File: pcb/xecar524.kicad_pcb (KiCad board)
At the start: 2 copper layers, 63.8 x 88.9 mm, 40 parts, among them J1 JTAG, J2 PROG, J3 Conn_02x02_Odd_Even, U1 MCP1703A-3302_SOT89, U2 Atari_XE_Cartridge_Connector, U3 XC95144XL-TQ100, U4 SST39VF040

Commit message: PCB: Exchange cfg signals
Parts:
- removed REF**: OSHW-Symbol_6.7x6mm_Copper, Symbol:OSHW-Symbol_6.7x6mm_Copper
- D1: value LED -> KP-2012SGC
- D2: value LED -> FYLS-0805URC
- D3: value LED -> KP-2012SYC
- R1: value 1k -> 100
- R14: value 1k -> 470
- R15: value 1k -> 220
- moved R16 2.54 mm to (140.1, 121.9)
- moved R17 2.54 mm to (140.1, 124.5)
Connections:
- J3 pad 1: CFG0 -> CFG1
- J3 pad 3: CFG1 -> CFG0
- U3 pad 37: CFG1 -> CFG0
- U3 pad 39: CFG0 -> CFG1
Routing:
- net CFG1: track 63.8 -> 63.2 mm
- net CFG0: track 63.2 -> 63.8 mm

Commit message: PCB: Resize
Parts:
- moved R14 1.54 mm to (126.0, 74.9)
- moved R15 1.54 mm to (126.0, 77.0)
- moved D1 0.78 mm to (121.2, 68.0)
- moved R1 0.75 mm to (121.2, 65.5)
- moved D2 0.70 mm to (121.2, 74.9)
- moved D3 0.70 mm to (121.2, 77.0)
- moved R2 0.53 mm to (133.8, 117.2)
- moved R3 0.53 mm to (133.8, 112.1)
- moved R4 0.53 mm to (133.8, 109.6)
- moved R5 0.53 mm to (133.8, 107.0)
- moved R6 0.53 mm to (133.8, 104.5)
- moved J2 0.50 mm to (127.0, 100.0)
- moved J1 0.50 mm to (127.0, 117.2)
- moved J3 0.46 mm to (132.5, 124.5)
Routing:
- net GND: track 50.8 -> 43.0 mm
- net +3V3: track 221.8 -> 219.0 mm
- net Net-(R15-Pad1): track 17.9 -> 16.4 mm
- net Net-(R14-Pad1): track 17.8 -> 16.2 mm
- net Net-(D3-Pad1): track 1.89 -> 2.72 mm
- net Net-(D2-Pad1): track 1.89 -> 2.72 mm
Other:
- board size 63.8 x 88.9 mm -> 62.8 x 89.4 mm

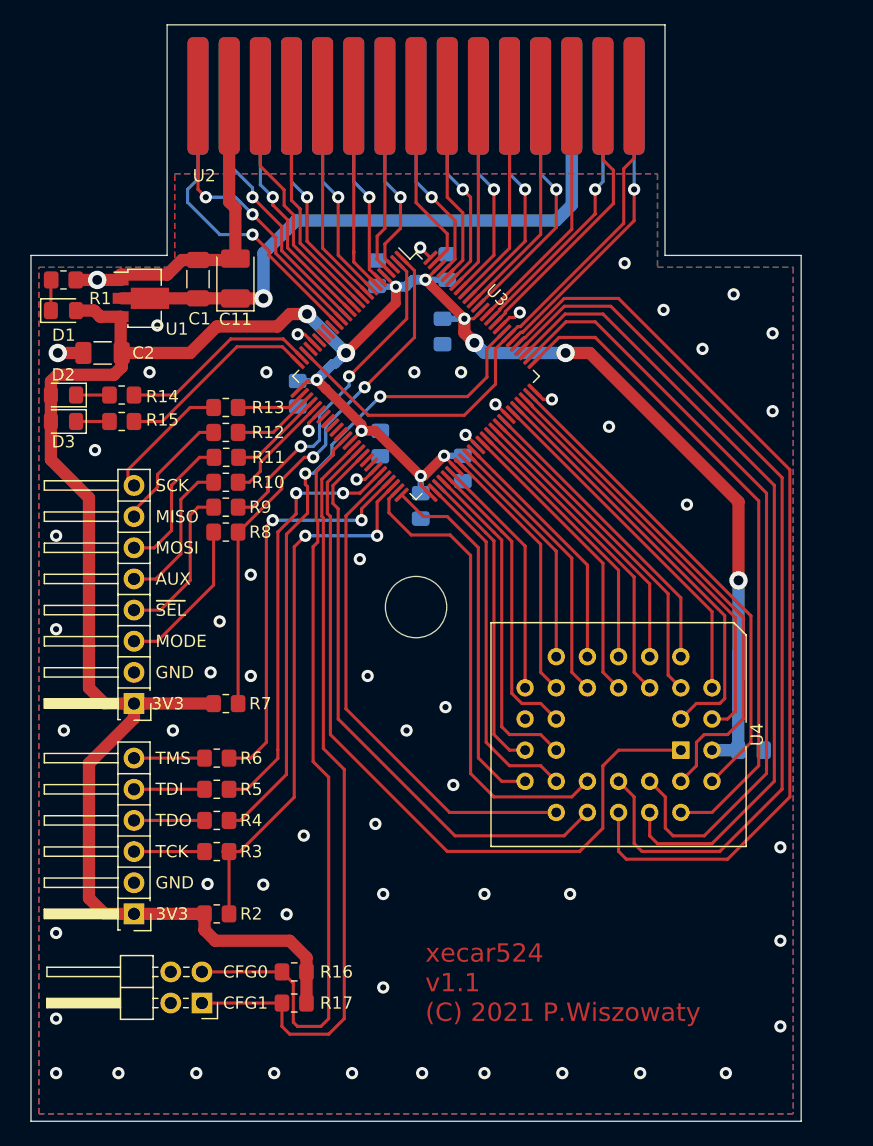
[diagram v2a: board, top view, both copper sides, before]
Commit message: PCB, PLD: Integrate R-Time 8 emulator
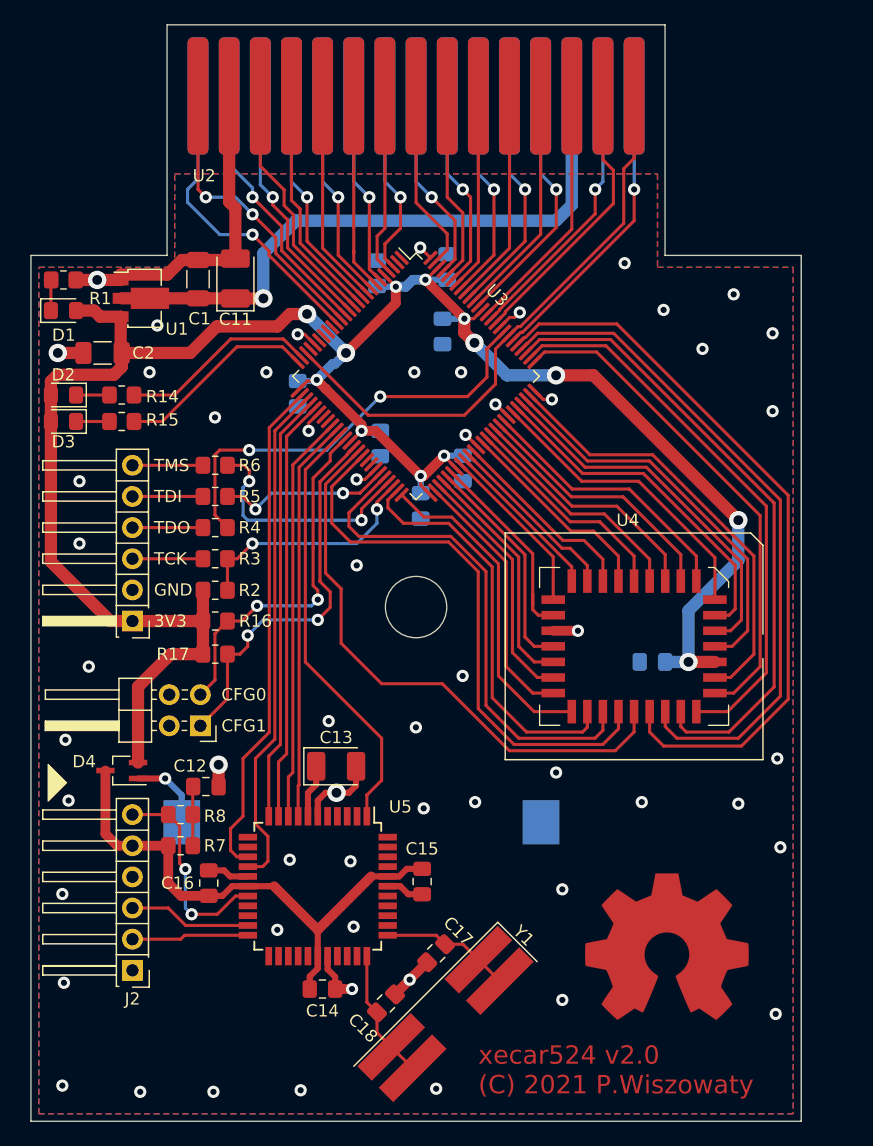
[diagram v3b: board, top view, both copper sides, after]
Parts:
- removed R10, R11, R12, R13, R9: 100, Resistor_SMD:R_0805_2012Metric_Pad1.20x1.40mm_HandSolder
- added BT1: CR2032, Miscellaneous:BatteryHolder_Connfly_DS1092-10, B.Cu at (145.5, 109.7)
- added C12: 100nF, Capacitor_SMD:C_0805_2012Metric_Pad1.18x1.45mm_HandSolder, F.Cu at (132.9, 106.8)
- added C13: 10uF, Capacitor_Tantalum_SMD:CP_EIA-3528-12_Kemet-T_Pad1.50x2.35mm_HandSolder, F.Cu at (143.5, 105.2)
- added C14: 100nF, Capacitor_SMD:C_0805_2012Metric_Pad1.18x1.45mm_HandSolder, F.Cu at (142.4, 123.3)
- added C15: 100nF, Capacitor_SMD:C_0805_2012Metric_Pad1.18x1.45mm_HandSolder, F.Cu at (150.5, 114.6)
- added C16: 100nF, Capacitor_SMD:C_0805_2012Metric_Pad1.18x1.45mm_HandSolder, F.Cu at (133.1, 114.7)
- added C17: 10pF, Capacitor_SMD:C_0805_2012Metric_Pad1.18x1.45mm_HandSolder, F.Cu at (151.6, 120.4)
- added C18: 10pF, Capacitor_SMD:C_0805_2012Metric_Pad1.18x1.45mm_HandSolder, F.Cu at (147.5, 124.5)
- added D4: 1PS70SB15, Package_TO_SOT_SMD:SOT-323_SC-70_Handsoldering, F.Cu at (126.0, 105.5)
- added REF**: OSHW-Symbol_13.4x12mm_Copper, Symbol:OSHW-Symbol_13.4x12mm_Copper, F.Cu at (170.4, 119.9)
- added U5: PIC24FJ32GA004-I/PT, Package_QFP:TQFP-44_10x10mm_P0.8mm, F.Cu at (142.0, 114.9)
- added Y1: 32768, Crystal:Crystal_SMD_SeikoEpson_MC406-4Pin_9.6x4.1mm_HandSoldering, F.Cu at (152.4, 125.3)
- J2: value PROG -> ICSP; footprint Connector_PinHeader_2.54mm:PinHeader_1x08_P2.54mm_Horizontal_HighProfile -> Connector_PinHeader_2.54mm:PinHeader_1x06_P2.54mm_Horizontal_HighProfile
- R15: value 220 -> 470
- R8: value 100 -> 470
- U4: footprint Package_LCC:PLCC-32_THT-Socket -> Miscellaneous:PLCC-32_SMD-Socket
- moved R16 29.3 mm to (133.6, 93.3), turned to 0 degrees
- moved R17 29.2 mm to (133.6, 96.0), turned to 0 degrees
- moved R2 26.4 mm to (133.6, 90.8)
- moved J1 23.9 mm to (126.9, 93.3)
- moved R3 23.9 mm to (133.6, 88.2)
- moved R5 23.9 mm to (133.6, 83.2)
- moved R4 23.9 mm to (133.6, 85.7)
- moved R6 23.9 mm to (133.6, 80.6)
- moved R8 23.3 mm to (130.8, 109.1), turned to 0 degrees
- moved J3 22.6 mm to (132.4, 101.9)
- moved J2 21.8 mm to (126.9, 121.8)
- moved R7 12.2 mm to (130.8, 111.6), turned to 0 degrees
- moved C9 10.8 mm to (169.3, 96.6), turned to 180 degrees
- moved U4 9.28 mm to (167.8, 95.4)
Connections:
- J2 pad 1: +3V3 -> Net-(J2-Pad1)
- J2 pad 2: GND -> PGC
- J2 pad 3: Net-(J2-Pad3) -> PGD
- J2 pad 4: Net-(J2-Pad4) -> GND
- J2 pad 5: Net-(J2-Pad5) -> VDD
- J2 pad 6: Net-(J2-Pad6) -> MCLR
- R7 pad 1: MODE -> VDD
- R7 pad 2: +3V3 -> Net-(C12-Pad1)
- R8 pad 1: MODE -> MCLR
- R8 pad 2: Net-(J2-Pad3) -> Net-(C12-Pad1)
- U3 pad 1: MODE -> Net-(U3-Pad1)
- U3 pad 2: SEL# -> Net-(U3-Pad2)
- U3 pad 27: SCK -> PMWR
- U3 pad 28: MISO -> PMCS1
- U3 pad 29: MOSI -> PMRD
- U3 pad 30: AUX -> PMD0
- U3 pad 34: Net-(U3-Pad34) -> PMD1
- U3 pad 35: Net-(U3-Pad35) -> PMD2
- U3 pad 36: Net-(U3-Pad36) -> PMD3
- U3 pad 40: ROM_A18 -> ROM_A11
- U3 pad 41: ROM_A10 -> OE#
- U3 pad 46: ROM_D7 -> ROM_A10
- U3 pad 49: OE# -> CE#
- U3 pad 50: ROM_D6 -> ROM_D7
- U3 pad 52: CE# -> ROM_D6
- U3 pad 53: ROM_D4 -> ROM_D5
- U3 pad 54: ROM_D5 -> ROM_D4
- U3 pad 56: ROM_D1 -> ROM_D2
- U3 pad 58: ROM_D2 -> ROM_D1
- U3 pad 73: WE# -> ROM_A18
- U3 pad 74: ROM_A17 -> WE#
- U3 pad 76: ROM_A14 -> ROM_A17
- U3 pad 77: ROM_A13 -> ROM_A14
- U3 pad 78: ROM_A8 -> ROM_A13
- U3 pad 79: ROM_A9 -> ROM_A8
- U3 pad 80: ROM_A11 -> ROM_A9
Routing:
- net VDD: track 0.00 -> 43.8 mm
- net MODE: track 43.2 -> 0.00 mm, vias 2 -> 0
- net PMCS1: track 0.00 -> 41.6 mm
- net PMWR: track 0.00 -> 41.2 mm
- net PMD3: track 0.00 -> 35.4 mm
- net +3V3: track 219.0 -> 183.8 mm, vias 12 -> 13
- net PMRD: track 0.00 -> 35.1 mm
- net PMD0: track 0.00 -> 34.5 mm
- net CFG0: track 63.3 -> 29.4 mm, vias 0 -> 2
- net PMD1: track 0.00 -> 33.4 mm
- net PMD2: track 0.00 -> 32.8 mm
- net CFG1: track 62.7 -> 31.8 mm, vias 0 -> 2
- net ROM_A18: track 63.1 -> 32.5 mm
- net ROM_A11: track 75.8 -> 47.1 mm
- net SEL#: track 27.7 -> 0.00 mm, vias 2 -> 0
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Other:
- board text added: "xecar524 v2.0 (C) 2021 P.Wiszowaty"
- board text removed: "AUX"
- board text removed: "MISO"
- board text removed: "MODE"
- board text removed: "MOSI"
- board text removed: "SCK"
- board text removed: "xecar524 v1.1 (C) 2021 P.Wiszowaty"
- board text removed: "~SEL~"

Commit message: PCB: Add connector for measuring deep sleep current
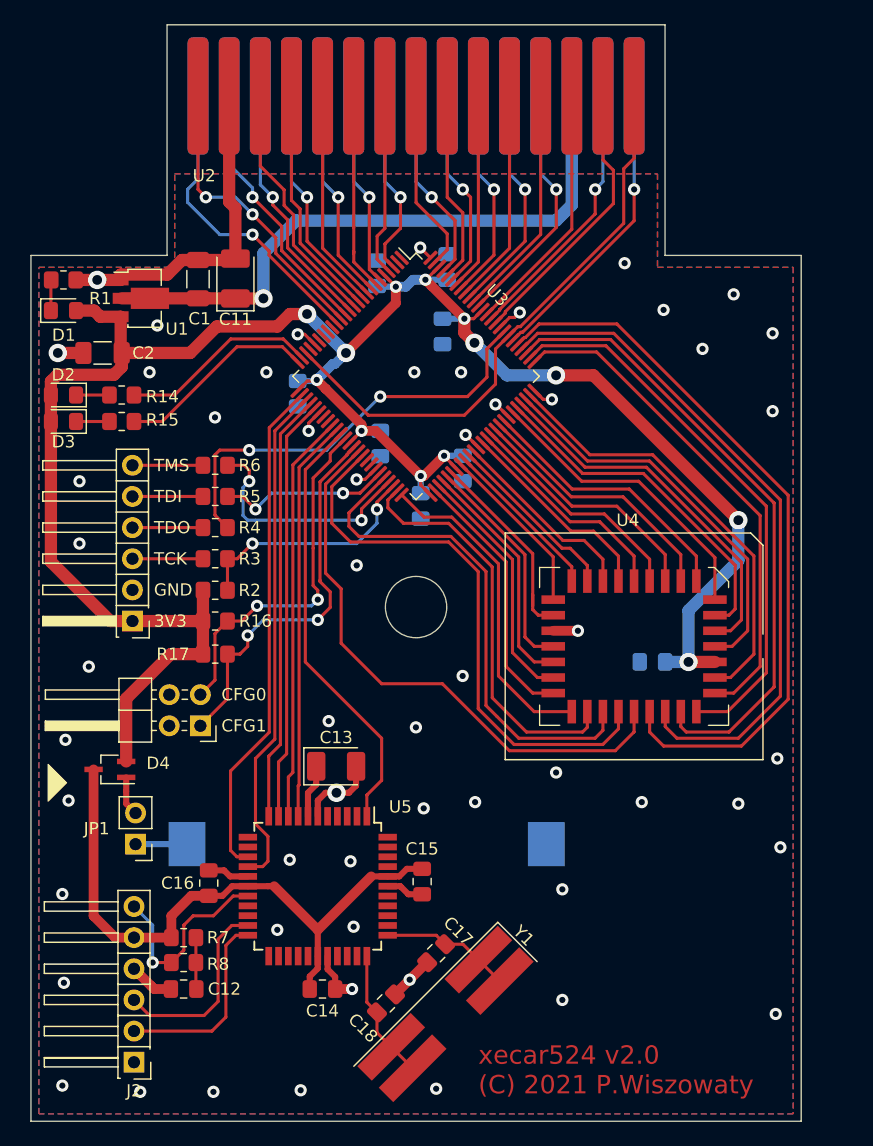
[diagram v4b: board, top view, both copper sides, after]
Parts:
- removed REF**: OSHW-Symbol_13.4x12mm_Copper, Symbol:OSHW-Symbol_13.4x12mm_Copper
- added JP1: Jumper_2_Bridged, Connector_PinHeader_2.54mm:PinHeader_1x02_P2.54mm_Vertical, F.Cu at (127.1, 111.5)
- C17, C18: value 10pF -> 15pF
- moved C12 16.6 mm to (131.0, 123.3), turned to 180 degrees
- moved R8 12.1 mm to (131.0, 121.2)
- moved R7 7.50 mm to (131.0, 119.1)
- moved J2 7.49 mm to (127.0, 129.3)
- moved BT1 1.83 mm to (146.0, 111.5)
- moved D4 0.97 mm to (125.0, 105.4)
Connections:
- D4 pad 1: Net-(BT1-Pad1) -> Net-(D4-Pad1)
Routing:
- net VDD: track 43.8 -> 50.9 mm
- net PGC: track 9.54 -> 15.9 mm
- net PGD: track 10.0 -> 15.8 mm
- net Net-(D4-Pad1): track 0.00 -> 3.22 mm
- net Net-(BT1-Pad1): track 6.35 -> 4.19 mm, vias 1 -> 0
- net GND: track 67.8 -> 69.7 mm, vias 57 -> 56
- net MCLR: track 17.0 -> 16.4 mm, vias 2 -> 1
- net Net-(C12-Pad1): track 4.84 -> 4.21 mm

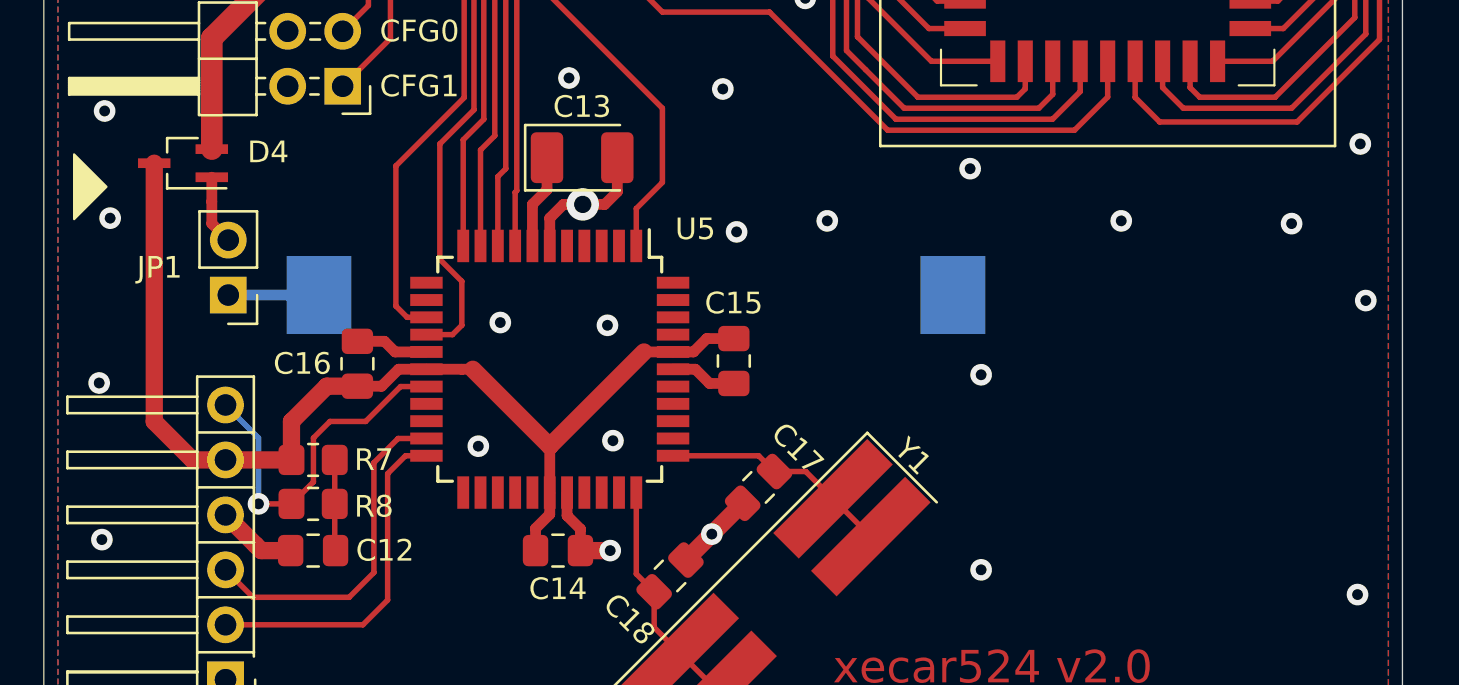
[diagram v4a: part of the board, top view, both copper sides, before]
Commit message: PCB: Add description to deep sleep current measurement connector, add OSHW symbol
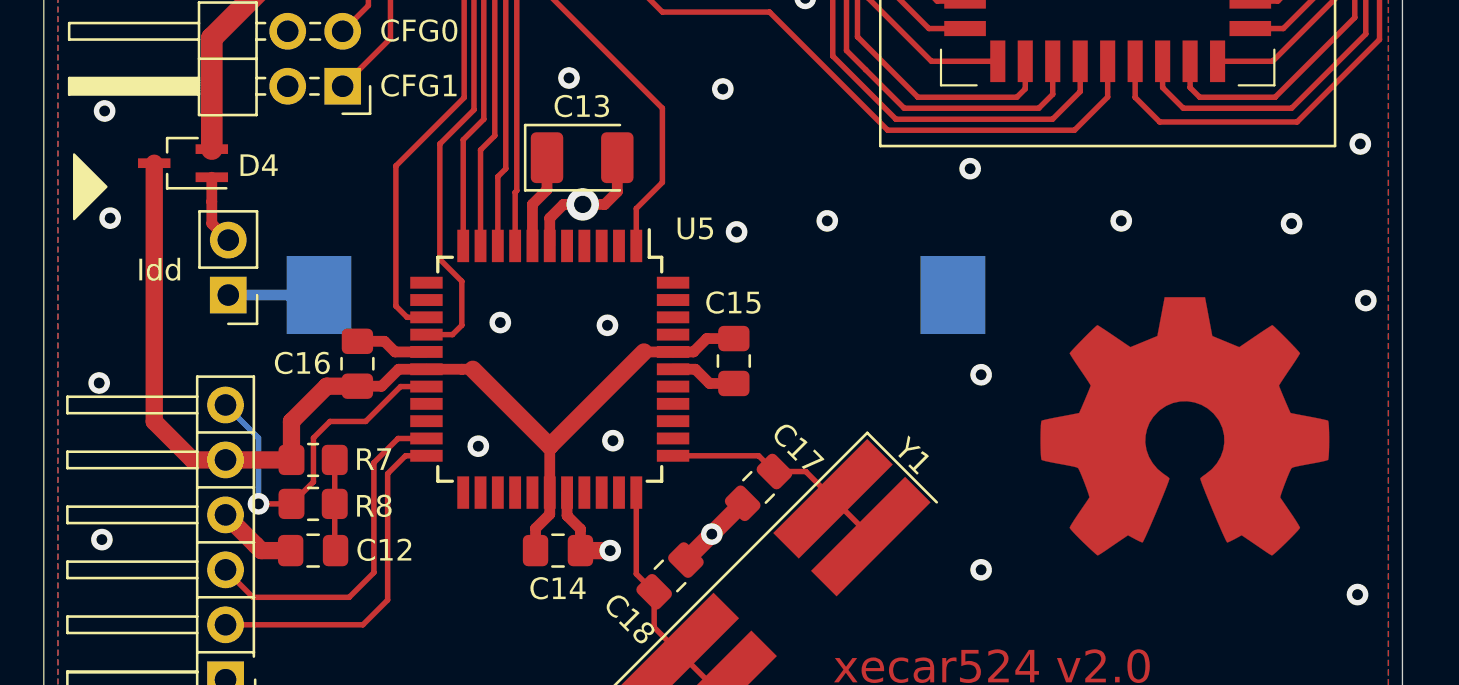
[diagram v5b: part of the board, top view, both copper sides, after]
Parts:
- added REF**: OSHW-Symbol_13.4x12mm_Copper, Symbol:OSHW-Symbol_13.4x12mm_Copper, F.Cu at (171.3, 117.6)
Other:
- board text added: "Idd"
